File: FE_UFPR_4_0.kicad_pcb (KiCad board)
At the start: 4 copper layers, 146.1 x 130 mm, 374 parts, among them J1 Mini-Fit Jr 5566-02A, J2 DSUB-37_Socket, J20 LaunchPad J1+J3, J21 LaunchPad J4+J2, J22 LaunchPad J5+J7, J23 LaunchPad J8+J6, J3 LEM DTM13-12PA-R005 key A, J4 ENC DTM13-12PB-R005 key B, J5 VEH DTM13-08PA-R004 key A, Q1 SQD50P06-15L, U1 LMR33630ADDAR, U10 SN74LVC2G17DBVR, U11 SN74LVC2G17DBVR, U12 OPA2376, U13 OPA2376, U14 OPA2376, U15 OPA2376, U16 OPA2376, U17 OPA2376, U18 SN65HVD230DR, U19 LTV-817S-TA1-C, U2 TPS62933FDRLR, U20 LTV-817S-TA1-C, U21 SN74LVC2G17DBVR, U3 AMS1117-3.3, U4 URA2415YMD-6WR3, U5 UCC27524DR, U6 UCC27524DR, U7 UCC27524DR, U8 SN74LVC1G11DBVR, U9 SN74LVC2G17DBVR

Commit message: Placing op amps part 1
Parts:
- moved TP30 190.9 mm to (-127.0, 194.4)
- moved TP31 190.9 mm to (-124.0, 194.4)
- moved C63 172.1 mm to (-91.9, 137.8), turned to -90 degrees
- moved R67 168.6 mm to (-95.1, 142.2)
- moved R74 166.0 mm to (-86.9, 138.3)
- moved C68 166.0 mm to (-83.2, 138.6)
- moved R63 165.8 mm to (-95.9, 137.8), turned to 90 degrees
- moved R66 163.0 mm to (-94.1, 137.8), turned to -90 degrees
- moved JP3 152.8 mm to (-77.5, 137.0), turned to 90 degrees
- moved C65 151.3 mm to (-82.4, 129.7)
- moved C66 151.3 mm to (-89.3, 132.5)
- moved C67 151.3 mm to (-85.8, 132.5)
- moved R68 151.3 mm to (-78.1, 130.1)
- moved R69 151.3 mm to (-73.1, 130.1)
- moved R70 151.3 mm to (-68.8, 129.7)
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
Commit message: Placing rest blocks
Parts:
- C113, C120, C25, C26, C27, C28, R118, R119: moved to B.Cu
- moved C112 288.7 mm to (208.8, 106.0), turned to 180 degrees
- moved C99 288.0 mm to (218.6, 119.5), turned to 90 degrees
- moved R110 285.2 mm to (216.4, 125.2), turned to 180 degrees
- moved TP41 283.5 mm to (185.3, 127.8)
- moved C66 282.3 mm to (183.5, 204.8), turned to 90 degrees
- moved R108 282.1 mm to (215.6, 120.3), turned to 180 degrees
- moved R109 281.8 mm to (215.6, 118.5), turned to 0 degrees
- moved C105 281.4 mm to (215.6, 116.7), turned to 0 degrees
- moved R63 281.1 mm to (180.3, 190.1), turned to -90 degrees
- moved R74 281.1 mm to (186.2, 204.9), turned to -90 degrees
- moved FB1 280.7 mm to (209.8, 103.0), turned to -90 degrees
- moved TP40 280.1 mm to (185.3, 124.2)
- moved R66 279.1 mm to (179.5, 192.8), turned to 180 degrees
- moved C106 278.8 mm to (213.2, 125.2), turned to 180 degrees
- moved C64 278.3 mm to (178.7, 190.1), turned to -90 degrees
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
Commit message: Finished placing tps
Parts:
- removed TP20: TP_VBUS_ADC, FE_UFPR_4_0:TestPoint_Pad_D1.5mm
- removed TP23: TP_NTC_ADC, FE_UFPR_4_0:TestPoint_Pad_D1.5mm
- removed TP37: ISO_COM, FE_UFPR_4_0:TestPoint_Pad_D1.5mm
- removed TP54: MOT_TEMP_REF, FE_UFPR_4_0:TestPoint_Pad_D1.5mm
- moved TP53 143.0 mm to (168.9, 138.9)
- moved TP34 125.4 mm to (190.2, 160.8)
- moved TP36 121.5 mm to (174.0, 149.5)
- moved TP35 121.5 mm to (190.2, 163.5)
- moved TP30 112.2 mm to (190.0, 186.5)
- moved TP31 108.7 mm to (189.8, 190.0)
- moved TP32 90.8 mm to (190.0, 175.0)
- moved TP43 90.4 mm to (185.0, 136.5)
- moved TP33 87.7 mm to (190.0, 178.2)
- moved TP42 84.4 mm to (185.0, 133.0)
- moved TP28 76.1 mm to (248.2, 183.2)
- moved C60 63.9 mm to (215.3, 207.7), turned to 180 degrees
- moved TP27 62.1 mm to (265.2, 183.2)
- moved TP26 61.9 mm to (261.8, 183.2)
- moved C58 61.8 mm to (221.7, 208.2), turned to 180 degrees
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
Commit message: FIxing errors
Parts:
- moved C99 49.6 mm to (169.0, 119.8), turned to 0 degrees
- moved C62 45.1 mm to (185.7, 150.6)
- moved C63 45.1 mm to (178.5, 149.5)
- moved C64 45.1 mm to (177.6, 145.0)
- moved C65 45.1 mm to (176.7, 161.3)
- moved C66 45.1 mm to (182.5, 159.7)
- moved C67 45.1 mm to (175.5, 151.7)
- moved C68 45.1 mm to (184.2, 163.4)
- moved JP3 45.1 mm to (185.2, 156.4)
- moved R63 45.1 mm to (179.3, 145.0)
- moved R64 45.1 mm to (181.0, 148.8)
- moved R65 45.1 mm to (183.8, 150.6)
- moved R66 45.1 mm to (178.5, 147.6)
- moved R67 45.1 mm to (176.0, 145.0)
- moved R68 45.1 mm to (174.7, 157.5)
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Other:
- board size 146.1 x 130 mm -> 146 x 130 mm

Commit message: Commiting jlc rules
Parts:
- moved C64 72.5 mm to (214.4, 207.5), turned to 90 degrees
- moved R67 70.7 mm to (214.4, 204.3), turned to 90 degrees
- moved R34 68.6 mm to (251.4, 217.3), turned to 90 degrees
- moved C70 53.0 mm to (212.2, 207.5), turned to 90 degrees
- moved R77 51.8 mm to (212.2, 204.3), turned to 90 degrees
- moved C38 49.3 mm to (247.2, 207.5)
- moved R25 47.8 mm to (247.2, 204.3)
- moved C37 44.6 mm to (243.6, 207.5), turned to 90 degrees
- moved R24 43.1 mm to (243.6, 204.3), turned to 90 degrees
- moved C40 42.1 mm to (241.8, 207.5)
- moved R27 38.6 mm to (241.8, 204.3)
- moved C39 36.5 mm to (238.2, 207.5), turned to 90 degrees
- moved R89 35.7 mm to (208.8, 204.3), turned to 90 degrees
- moved C77 35.6 mm to (208.8, 207.5), turned to 90 degrees
- moved C79 35.3 mm to (169.0, 172.0)
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
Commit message: More routing
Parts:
- NT2: moved to B.Cu
- moved R57 49.1 mm to (222.0, 199.1)
- moved R58 48.0 mm to (219.2, 199.2)
- moved R59 46.0 mm to (219.2, 195.7)
- moved R60 45.3 mm to (216.0, 195.5)
- moved R61 45.3 mm to (213.5, 194.7)
- moved R62 45.3 mm to (211.1, 195.6)
- moved C35 5.48 mm to (243.3, 145.2), turned to 0 degrees
- moved C98 4.25 mm to (171.5, 108.0)
- moved NT2 1.85 mm to (251.8, 97.2)
- moved R32 0.75 mm to (243.3, 143.8)
- moved R33 0.65 mm to (243.3, 146.8)
- turned R16 to 180 degrees
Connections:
- D2 pad 1: +24V_PROT -> /power/PWR_QGATE
- D2 pad 2: /power/PWR_QGATE -> (no net)
- D2 pad 3: (no net) -> +24V_PROT
- R18 pad 1: /gate_drive/PWM_UH_DRV -> /gate_drive/PWM_UL_DRV
- R18 pad 2: /gate_drive/PWM_UH_15V -> /gate_drive/PWM_UL_15V
- R19 pad 1: /gate_drive/PWM_UL_DRV -> /gate_drive/PWM_UH_DRV
- R19 pad 2: /gate_drive/PWM_UL_15V -> /gate_drive/PWM_UH_15V
- R20 pad 1: /gate_drive/PWM_VH_DRV -> /gate_drive/PWM_VL_DRV
- R20 pad 2: /gate_drive/PWM_VH_15V -> /gate_drive/PWM_VL_15V
- R21 pad 1: /gate_drive/PWM_VL_DRV -> /gate_drive/PWM_VH_DRV
- R21 pad 2: /gate_drive/PWM_VL_15V -> /gate_drive/PWM_VH_15V
- R22 pad 1: /gate_drive/PWM_WH_DRV -> /gate_drive/PWM_WL_DRV
- R22 pad 2: /gate_drive/PWM_WH_15V -> /gate_drive/PWM_WL_15V
- R23 pad 1: /gate_drive/PWM_WL_DRV -> /gate_drive/PWM_WH_DRV
- R23 pad 2: /gate_drive/PWM_WL_15V -> /gate_drive/PWM_WH_15V
- R36 pad 1: /PWM_UH_3V3 -> /PWM_UL_3V3
- R37 pad 1: /PWM_UL_3V3 -> /PWM_UH_3V3
- R38 pad 1: /PWM_VH_3V3 -> /PWM_VL_3V3
- R39 pad 1: /PWM_VL_3V3 -> /PWM_VH_3V3
- R40 pad 1: /PWM_WH_3V3 -> /PWM_WL_3V3
- R41 pad 1: /PWM_WL_3V3 -> /PWM_WH_3V3
- U5 pad 2: /PWM_UH_3V3 -> /PWM_UL_3V3
- U5 pad 4: /PWM_UL_3V3 -> /PWM_UH_3V3
- U5 pad 5: /gate_drive/PWM_UL_DRV -> /gate_drive/PWM_UH_DRV
- U5 pad 7: /gate_drive/PWM_UH_DRV -> /gate_drive/PWM_UL_DRV
- U6 pad 2: /PWM_VH_3V3 -> /PWM_VL_3V3
- U6 pad 4: /PWM_VL_3V3 -> /PWM_VH_3V3
- U6 pad 5: /gate_drive/PWM_VL_DRV -> /gate_drive/PWM_VH_DRV
- U6 pad 7: /gate_drive/PWM_VH_DRV -> /gate_drive/PWM_VL_DRV
- U7 pad 2: /PWM_WH_3V3 -> /PWM_WL_3V3
- U7 pad 4: /PWM_WL_3V3 -> /PWM_WH_3V3
- U7 pad 5: /gate_drive/PWM_WL_DRV -> /gate_drive/PWM_WH_DRV
- U7 pad 7: /gate_drive/PWM_WH_DRV -> /gate_drive/PWM_WL_DRV
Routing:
- net +24V_PROT: track 0.00 -> 186.3 mm, vias 0 -> 2
- net PGND_MOD: track 0.00 -> 176.0 mm, vias 0 -> 1
- net /gate_drive/SHIELD_DB37: track 0.00 -> 90.4 mm
- net /encoder/MOT_TEMP_RAW: track 0.00 -> 41.3 mm
- net /vehicle_io/CAN_L_XCVR: track 0.00 -> 37.4 mm
- net /vehicle_io/CAN_L: track 0.00 -> 33.5 mm
- net /vehicle_io/CAN_H_XCVR: track 0.00 -> 33.4 mm
- net +3V3: track 0.00 -> 32.3 mm
- net /vehicle_io/CAN_H: track 0.00 -> 31.7 mm
- net /encoder/ENC_VDD: track 0.00 -> 27.5 mm
- net +15V_ISO: track 0.00 -> 24.3 mm
- net /vehicle_io/+5V_VEH: track 0.00 -> 23.8 mm
- net ISO_COM: track 0.00 -> 23.3 mm
- net +5V: track 0.00 -> 22.4 mm
- net -15V_ISO: track 0.00 -> 21.3 mm
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- added copper zone on B.Cu, net ISO_COM
- added copper zone on F.Cu, net ISO_COM

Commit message: CONTINUING ROUTING
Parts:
- moved C33 11.3 mm to (228.6, 169.0), turned to 0 degrees
- moved C32 9.48 mm to (228.4, 161.4), turned to 0 degrees
- moved C31 9.39 mm to (228.6, 159.6), turned to 0 degrees
- moved C36 9.12 mm to (229.1, 157.2)
- moved C29 8.18 mm to (228.4, 178.3), turned to 0 degrees
- moved C34 8.08 mm to (228.3, 170.8), turned to 0 degrees
- moved C30 7.31 mm to (228.2, 180.2), turned to 0 degrees
- moved R19 6.52 mm to (222.8, 163.1)
- moved R18 5.56 mm to (222.7, 165.7)
- moved R93 4.71 mm to (174.6, 205.0)
- moved R69 4.70 mm to (174.5, 159.9)
- moved R81 4.70 mm to (174.6, 182.2)
- moved R37 4.30 mm to (232.6, 162.3), turned to 90 degrees
- moved R40 3.92 mm to (232.4, 183.8)
- moved R21 3.62 mm to (222.5, 172.4)
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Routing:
- net +13V5_GATE: track 10.1 -> 41.6 mm
- net /encoder/ENC_COS_P: track 0.00 -> 8.14 mm
- net /current_sense/ISNS_C_INT_N: track 0.00 -> 7.08 mm
- net /current_sense/ISNS_A_INT_N: track 0.00 -> 7.08 mm
- net /current_sense/ISNS_B_INT_N: track 0.00 -> 7.08 mm
- net /current_sense/ISNS_B_LEM_N: track 0.00 -> 6.64 mm
- net /current_sense/ISNS_C_LEM_P: track 0.00 -> 6.60 mm
- net /encoder/ENC_SIN_P: track 0.00 -> 6.34 mm
- net /current_sense/ISNS_B_INT_P: track 0.00 -> 5.96 mm
- net /current_sense/ISNS_B_LEM_P: track 0.00 -> 5.93 mm
- net /current_sense/ISNS_A_LEM_P: track 0.00 -> 5.93 mm
- net /current_sense/LEM_C_M: track 17.7 -> 12.8 mm
- net /PWM_WL_3V3: track 7.10 -> 10.8 mm
- net /current_sense/LEM_A_M: track 18.0 -> 14.4 mm
- net /PWM_WH_3V3: track 7.40 -> 10.2 mm
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
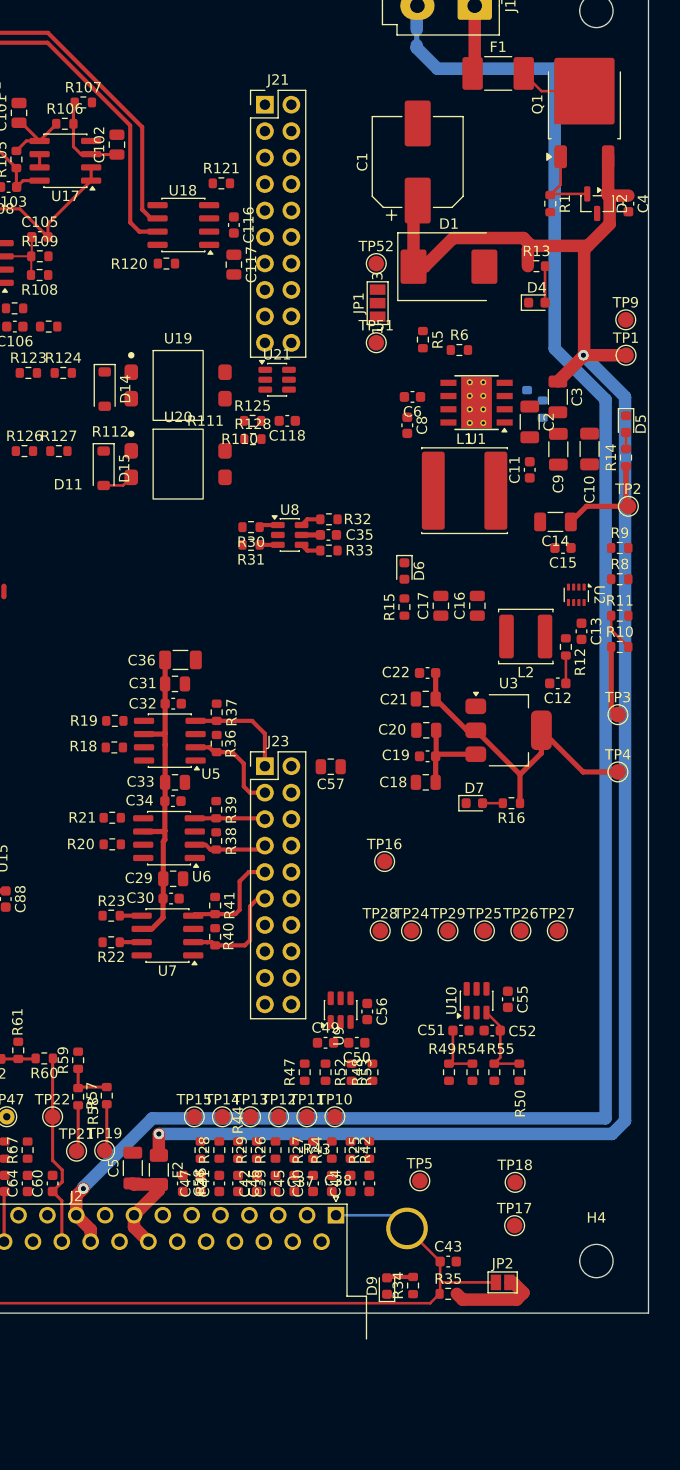
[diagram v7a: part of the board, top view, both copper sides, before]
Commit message: Remade driver connections
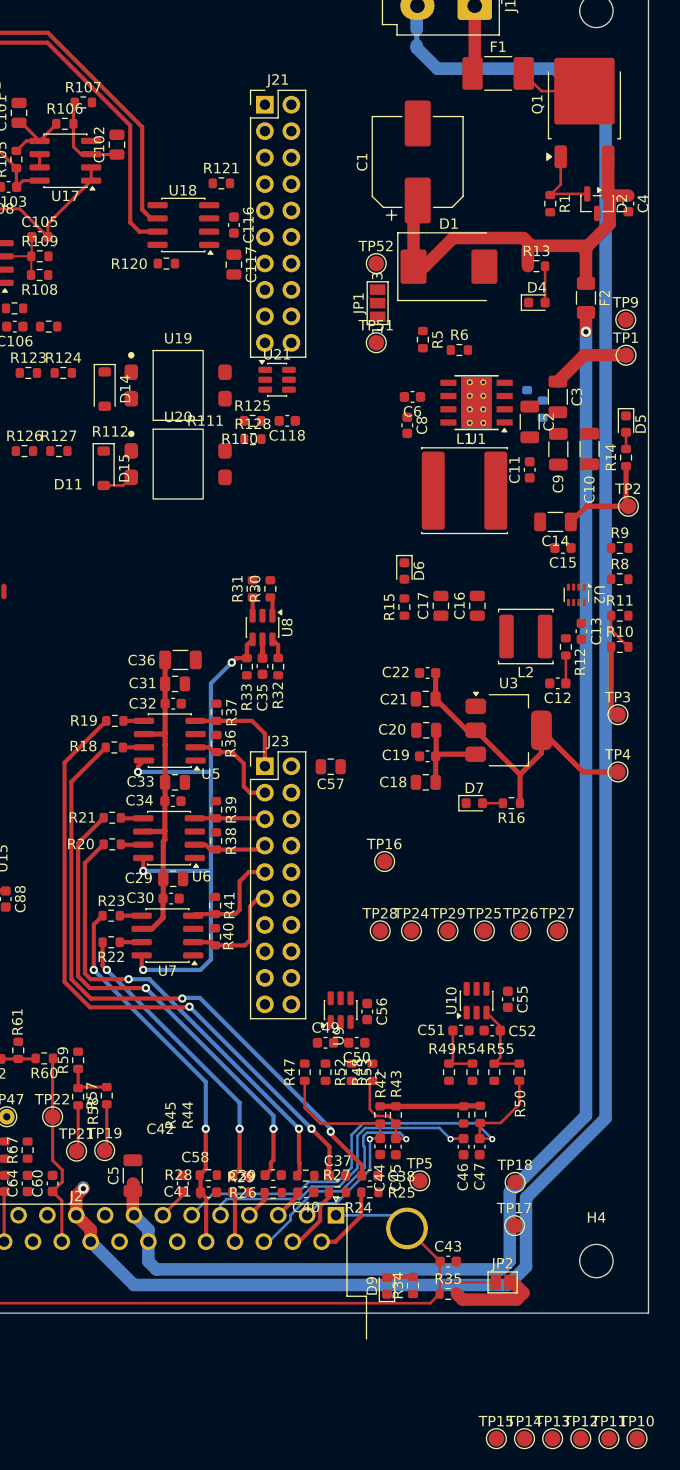
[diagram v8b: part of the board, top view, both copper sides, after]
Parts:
- moved F2 93.2 mm to (268.0, 122.5)
- moved TP14 42.4 mm to (262.1, 232.0)
- moved TP11 42.4 mm to (270.2, 232.0)
- moved TP12 42.4 mm to (267.5, 232.0)
- moved TP13 42.4 mm to (264.8, 232.0)
- moved TP10 42.4 mm to (272.9, 232.0)
- moved TP15 42.4 mm to (259.4, 232.0)
- moved R45 27.1 mm to (257.9, 200.9)
- moved C47 27.0 mm to (257.8, 204.0), turned to -90 degrees
- moved C46 21.9 mm to (256.2, 204.0), turned to -90 degrees
- moved R44 21.9 mm to (256.2, 200.9)
- moved R32 15.0 mm to (238.4, 157.9), turned to -90 degrees
- moved C35 14.1 mm to (236.9, 157.8), turned to -90 degrees
- moved R33 13.7 mm to (235.4, 157.9), turned to -90 degrees
- moved C45 10.4 mm to (249.8, 204.0), turned to -90 degrees
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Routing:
- net +24V_PROT: track 186.3 -> 57.3 mm, vias 2 -> 0
- net +24V_MOD: track 9.60 -> 136.9 mm, vias 0 -> 1
- net /gate_drive/PWM_UH_15V: track 0.00 -> 69.3 mm, vias 0 -> 2
- net /gate_drive/PWM_UL_15V: track 0.00 -> 67.6 mm, vias 0 -> 2
- net /gate_drive/GATE_EN_3V3: track 2.17 -> 57.6 mm, vias 0 -> 4
- net /gate_drive/PWM_VH_15V: track 0.00 -> 49.8 mm, vias 0 -> 2
- net /gate_drive/PWM_VL_15V: track 0.00 -> 48.0 mm, vias 0 -> 2
- net /FLT_OT_15V: track 0.00 -> 44.5 mm, vias 0 -> 1
- net /gate_drive/PWM_WH_15V: track 0.00 -> 37.0 mm, vias 0 -> 2
- net /gate_drive/PWM_WL_15V: track 0.00 -> 33.1 mm, vias 0 -> 2
- net /FLT_OC_C_15V: track 0.00 -> 29.7 mm, vias 0 -> 1
- net /FLT_OC_B_15V: track 0.00 -> 28.9 mm, vias 0 -> 1
- net /FLT_OC_A_15V: track 0.00 -> 23.7 mm, vias 0 -> 1
- net +13V5_GATE: track 41.6 -> 51.2 mm
- net PGND_MOD: track 176.0 -> 184.8 mm
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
